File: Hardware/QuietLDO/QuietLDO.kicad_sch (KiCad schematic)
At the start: 95 parts

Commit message: start QuietPCB
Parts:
- added hole1, hole2, hole3, hole4: ~, persional_library:m3 125x300, symbol persional_library:Hole_M3-M
- C1, C10, C11, C12, C13, C14, C15, C16, C17, C18, C19, C2, C20, C21, C22, C23, C24, C25, C26, C27, C28, C29, C3, C30, C31, C32, C37, C4, C5, C6, C7, C8, C9: footprint persional_library:C0805 -> persional_library:C0603; symbol persional_library:C0805 -> persional_library:C0603; LCSC Part Name 22uF ±20% 25V -> 1uF ±10% 50V; Manufacturer Part CL21A226MAQNNNE -> CL10A105KB8NNNC; Supplier Part C45783 -> C15849
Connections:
- net +1V8: now also CN15.2, CN7.2, U3.20 (OUT); no longer CN15.1, CN7.1
- net +3V3: now also CN10.2, CN4.2, U2.20 (OUT); no longer CN10.1, CN4.1
- net +5V: now also CN13.2, CN3.2; no longer CN13.1, CN3.1, U2.20 (OUT), U3.20 (OUT), U4.20 (OUT)
- net GND: now also CN10.1, CN13.1, CN15.1, CN16.1, CN3.1, CN4.1, CN7.1, CN8.1, hole1.1 (GND), hole2.1 (GND), hole3.1 (GND), hole4.1 (GND); no longer CN10.2, CN13.2, CN15.2, CN16.2, CN3.2, CN4.2, CN7.2, CN8.2
- net VDD: now also CN16.2, CN8.2, U4.20 (OUT); no longer CN16.1, CN8.1
- net VIN: now also SW1.3; no longer SW1.1

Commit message: add QuietLDO PCB
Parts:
- R1, R11, R12, R14, R15, R16, R17, R18, R2, R20, R21, R22, R23, R24, R4, R5, R7, R8: value 0Ω -> NC
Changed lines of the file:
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@@
 			)
 		)
-		(property "Value" "0Ω"
+		(property "Value" "NC"
 			(at 80.01 64.77 0)
 			(effects
@@
 			)
 		)
-		(property "Value" "0Ω"
+		(property "Value" "NC"
 			(at 80.01 54.61 0)
 			(effects
@@
 			)
 		)
-		(property "Value" "0Ω"
+		(property "Value" "NC"
 			(at 167.64 54.61 0)
 			(effects
@@
 			)
 		)
-		(property "Value" "0Ω"
+		(property "Value" "NC"
 			(at 80.01 49.53 0)
 			(effects
@@
 			)
 		)
-		(property "Value" "0Ω"
+		(property "Value" "NC"
 			(at 80.01 62.23 0)
 			(effects
@@
 			)
 		)
-		(property "Value" "0Ω"
+		(property "Value" "NC"
 			(at 167.64 62.23 0)
 			(effects
@@
 			)
 		)
-		(property "Value" "0Ω"
+		(property "Value" "NC"
 			(at 80.01 115.57 0)
 			(effects
@@
 			)
 		)
-		(property "Value" "0Ω"
+		(property "Value" "NC"
 			(at 80.01 123.19 0)
 			(effects
@@
 			)
 		)
-		(property "Value" "0Ω"
+		(property "Value" "NC"
 			(at 80.01 57.15 0)
 			(effects
@@
 			)
 		)
-		(property "Value" "0Ω"
+		(property "Value" "NC"
 			(at 167.64 52.07 0)
 			(effects
@@
 			)
 		)
-		(property "Value" "0Ω"
+		(property "Value" "NC"
 			(at 167.64 59.69 0)
 			(effects
@@
 			)
 		)
-		(property "Value" "0Ω"
+		(property "Value" "NC"
 			(at 80.01 107.95 0)
 			(effects
@@
 			)
 		)
-		(property "Value" "0Ω"
+		(property "Value" "NC"
 			(at 167.64 64.77 0)
 			(effects
@@
 			)
 		)
-		(property "Value" "0Ω"
+		(property "Value" "NC"
 			(at 80.01 110.49 0)
 			(effects
@@
 			)
 		)
-		(property "Value" "0Ω"
+		(property "Value" "NC"
 			(at 80.01 125.73 0)
 			(effects
@@
 			)
 		)
-		(property "Value" "0Ω"
+		(property "Value" "NC"
 			(at 80.01 46.99 0)
 			(effects
@@
 			)
 		)
-		(property "Value" "0Ω"
+		(property "Value" "NC"
 			(at 80.01 120.65 0)
 			(effects
@@
 			)
 		)
-		(property "Value" "0Ω"
+		(property "Value" "NC"
 			(at 80.01 118.11 0)
 			(effects

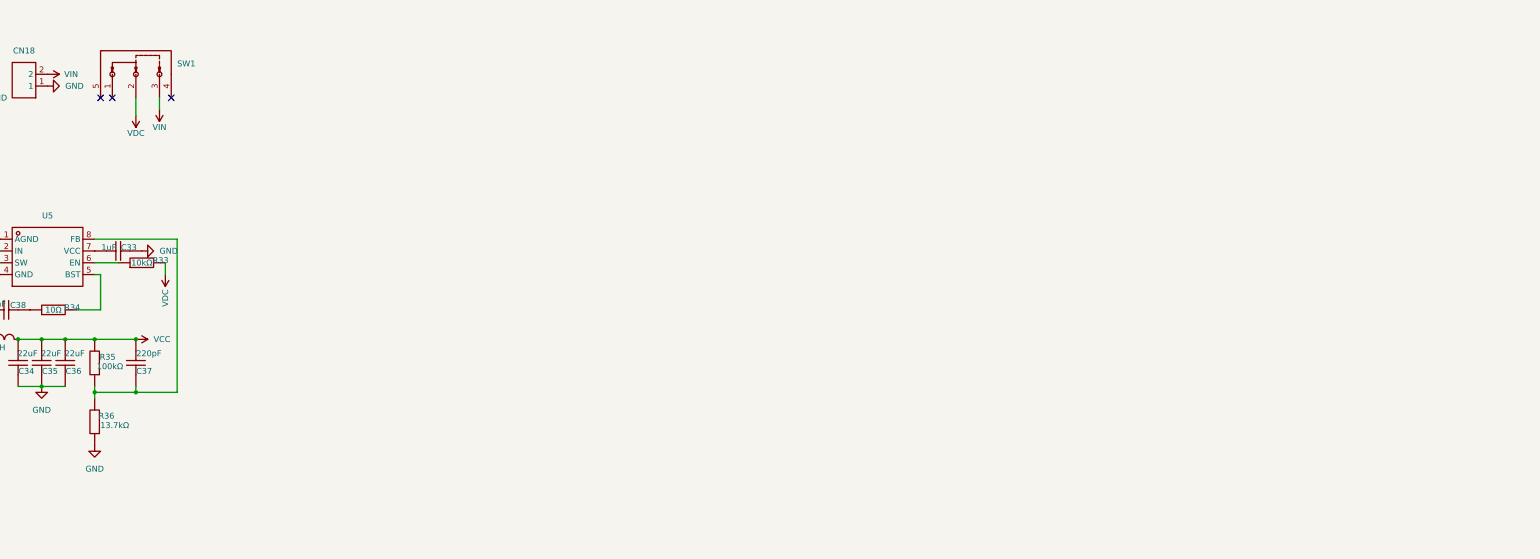
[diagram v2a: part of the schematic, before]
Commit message: add BOM Checklist Function
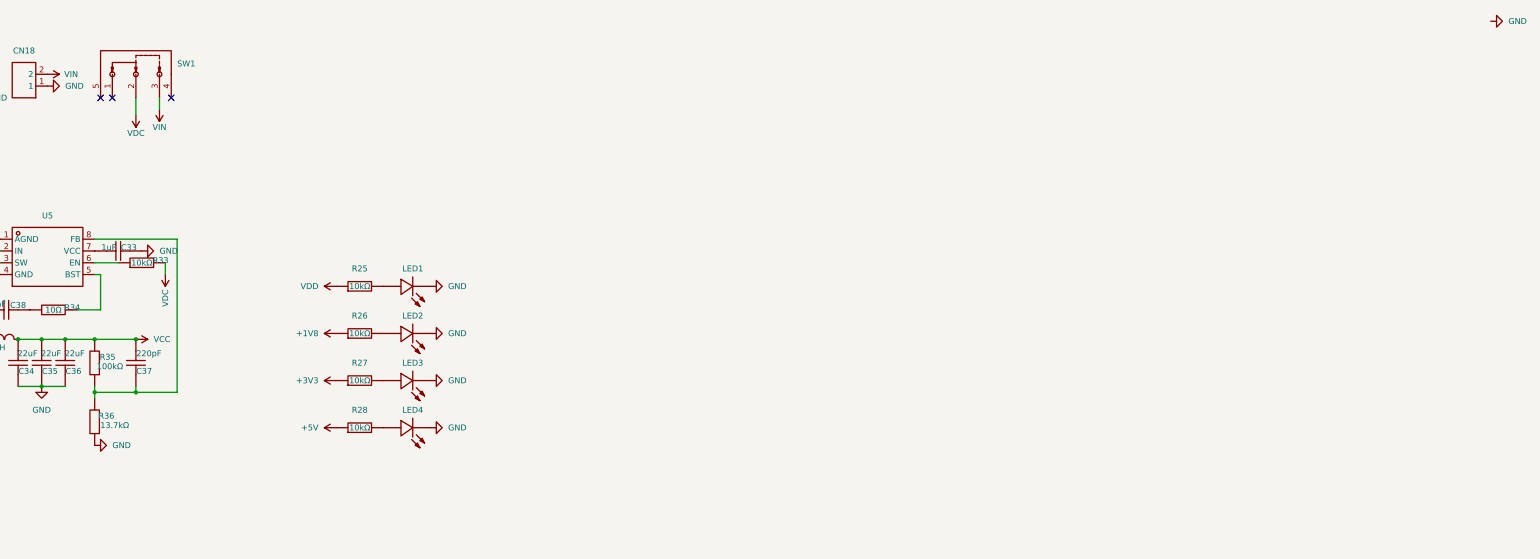
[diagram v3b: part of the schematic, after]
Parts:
- added LED1, LED2, LED3, LED4: ~, persional_library:LED0603-RD, symbol persional_library:LED0603
- added R25, R26, R27, R28: 10kΩ, persional_library:R0603, symbol persional_library:R0603
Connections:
- net +1V8: now also R26.1
- net +3V3: now also R27.1
- net +5V: now also R28.1
- net GND: now also LED1.1 (-), LED2.1 (-), LED3.1 (-), LED4.1 (-)
- net VDD: now also R25.1
- new net: LED4.2 (+), R28.2
- new net: LED2.2 (+), R26.2
- new net: LED1.2 (+), R25.2
- new net: LED3.2 (+), R27.2
